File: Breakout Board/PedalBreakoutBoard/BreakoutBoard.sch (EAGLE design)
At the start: 2 parts, among them U1 ES_DAISY_SEED_REV4, X1 5566-8

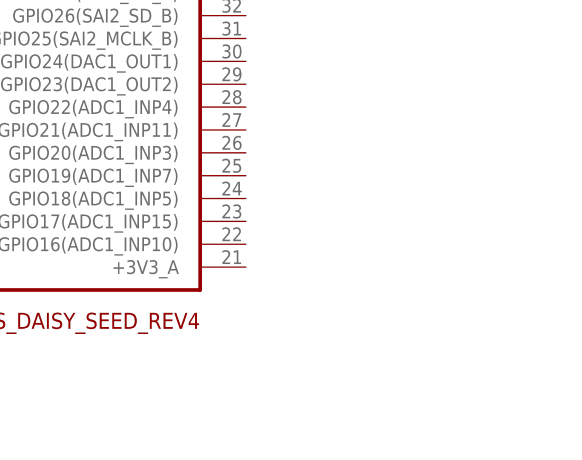
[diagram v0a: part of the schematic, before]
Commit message: DP-16 - Add LED molex
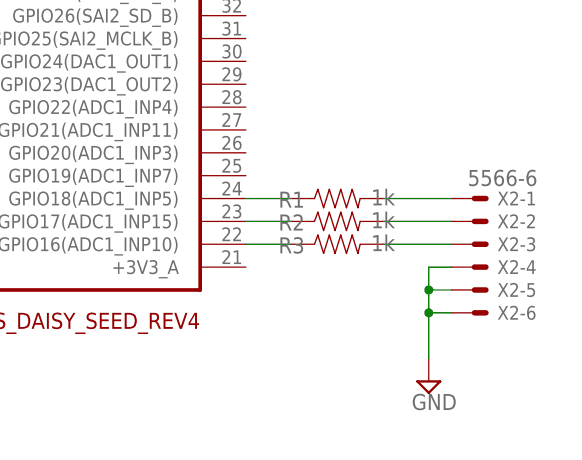
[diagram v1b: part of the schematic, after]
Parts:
- added R1, R2, R3: 1k, SparkFun-Resistors:1KOHM-HORIZ-1/4W-5%
- added X2: 5566-6, con-molex:5566-6
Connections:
- new net N$10: R3.2, X2-3.S
- new net N$5: R1.1, U1.GPIO18(ADC1_INP5)
- new net N$6: R2.1, U1.GPIO17(ADC1_INP15)
- new net N$7: R3.1, U1.GPIO16(ADC1_INP10)
- new net N$8: R1.2, X2-1.S
- new net N$9: R2.2, X2-2.S
- net GND: now also X2-4.S, X2-5.S, X2-6.S
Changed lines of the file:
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@@
 <groups>
 <schematic_group name="AUDIO_MOLEX"/>
+<schematic_group name="LED_MOLEX"/>
 </groups>
 <parts>
@@
 <part name="X1" library="con-molex" library_urn="urn:adsk.eagle:library:165" deviceset="5566-8" device="" package3d_urn="urn:adsk.eagle:package:8078580/1"/>
 <part name="SUPPLY3" library="supply2" library_urn="urn:adsk.eagle:library:372" deviceset="GND" device=""/>
+<part name="X2" library="con-molex" library_urn="urn:adsk.eagle:library:165" deviceset="5566-6" device="" package3d_urn="urn:adsk.eagle:package:8078581/1"/>
+<part name="SUPPLY4" library="supply2" library_urn="urn:adsk.eagle:library:372" deviceset="GND" device=""/>
+<part name="R1" library="SparkFun-Resistors" library_urn="urn:adsk.eagle:library:532" deviceset="1KOHM" device="-HORIZ-1/4W-5%" package3d_urn="urn:adsk.eagle:package:39658/1" value="1k"/>
+<part name="R2" library="SparkFun-Resistors" library_urn="urn:adsk.eagle:library:532" deviceset="1KOHM" device="-HORIZ-1/4W-5%" package3d_urn="urn:adsk.eagle:package:39658/1" value="1k"/>
+<part name="R3" library="SparkFun-Resistors" library_urn="urn:adsk.eagle:library:532" deviceset="1KOHM" device="-HORIZ-1/4W-5%" package3d_urn="urn:adsk.eagle:package:39658/1" value="1k"/>
 </parts>
 <sheets>
@@
 <instance part="SUPPLY3" gate="GND" x="50.8" y="50.8" smashed="yes">
 <attribute name="VALUE" x="48.895" y="47.625" size="1.778" layer="96"/>
+</instance>
+<instance part="X2" gate="-1" x="160.02" y="73.66" smashed="yes" grouprefs="LED_MOLEX">
+<attribute name="NAME" x="162.56" y="72.898" size="1.524" layer="95"/>
+<attribute name="VALUE" x="159.258" y="75.057" size="1.778" layer="96"/>
+</instance>
+<instance part="X2" gate="-2" x="160.02" y="71.12" smashed="yes" grouprefs="LED_MOLEX">
+<attribute name="NAME" x="162.56" y="70.358" size="1.524" layer="95"/>
+</instance>
+<instance part="X2" gate="-3" x="160.02" y="68.58" smashed="yes" grouprefs="LED_MOLEX">
+<attribute name="NAME" x="162.56" y="67.818" size="1.524" layer="95"/>
+</instance>
+<instance part="X2" gate="-4" x="160.02" y="66.04" smashed="yes" grouprefs="LED_MOLEX">
+<attribute name="NAME" x="162.56" y="65.278" size="1.524" layer="95"/>
+</instance>
+<instance part="X2" gate="-5" x="160.02" y="63.5" smashed="yes" grouprefs="LED_MOLEX">
+<attribute name="NAME" x="162.56" y="62.738" size="1.524" layer="95"/>
+</instance>
+<instance part="X2" gate="-6" x="160.02" y="60.96" smashed="yes" grouprefs="LED_MOLEX">
+<attribute name="NAME" x="162.56" y="60.198" size="1.524" layer="95"/>
+</instance>
+<instance part="SUPPLY4" gate="GND" x="154.94" y="53.34" smashed="yes">
+<attribute name="VALUE" x="153.035" y="50.165" size="1.778" layer="96"/>
+</instance>
+<instance part="R1" gate="G$1" x="144.78" y="73.66" smashed="yes">
+<attribute name="NAME" x="139.7" y="72.644" size="1.778" layer="95" font="vector" align="bottom-center"/>
+<attribute name="VALUE" x="149.86" y="74.676" size="1.778" layer="96" font="vector" align="top-center"/>
+</instance>
+<instance part="R2" gate="G$1" x="144.78" y="71.12" smashed="yes">
+<attribute name="NAME" x="139.7" y="70.104" size="1.778" layer="95" font="vector" align="bottom-center"/>
+<attribute name="VALUE" x="149.86" y="72.136" size="1.778" layer="96" font="vector" align="top-center"/>
+</instance>
+<instance part="R3" gate="G$1" x="144.78" y="68.58" smashed="yes">
+<attribute name="NAME" x="139.7" y="67.564" size="1.778" layer="95" font="vector" align="bottom-center"/>
+<attribute name="VALUE" x="149.86" y="69.596" size="1.778" layer="96" font="vector" align="top-center"/>
 </instance>
 </instances>
@@
 <junction x="50.8" y="63.5"/>
 </segment>
+<segment>
+<pinref part="X2" gate="-6" pin="S"/>
+<wire x1="157.48" y1="60.96" x2="154.94" y2="60.96" width="0.1524" layer="91"/>
+<pinref part="SUPPLY4" gate="GND" pin="GND"/>
+<wire x1="154.94" y1="60.96" x2="154.94" y2="55.88" width="0.1524" layer="91"/>
+<pinref part="X2" gate="-5" pin="S"/>
+<wire x1="157.48" y1="63.5" x2="154.94" y2="63.5" width="0.1524" layer="91"/>
+<wire x1="154.94" y1="63.5" x2="154.94" y2="60.96" width="0.1524" layer="91"/>
+<junction x="154.94" y="60.96"/>
+<pinref part="X2" gate="-4" pin="S"/>
+<wire x1="157.48" y1="66.04" x2="154.94" y2="66.04" width="0.1524" layer="91"/>
+<wire x1="154.94" y1="66.04" x2="154.94" y2="63.5" width="0.1524" layer="91"/>
+<junction x="154.94" y="63.5"/>
+</segment>
 </net>
 <net name="N$1" class="0">
@@
 </segment>
 </net>
+<net name="N$5" class="0">
+<segment>
+<pinref part="U1" gate="G$1" pin="GPIO18(ADC1_INP5)"/>
+<pinref part="R1" gate="G$1" pin="1"/>
+<wire x1="134.62" y1="73.66" x2="139.7" y2="73.66" width="0.1524" layer="91"/>
+</segment>
+</net>
+<net name="N$6" class="0">
+<segment>
+<pinref part="U1" gate="G$1" pin="GPIO17(ADC1_INP15)"/>
+<pinref part="R2" gate="G$1" pin="1"/>
+<wire x1="134.62" y1="71.12" x2="139.7" y2="71.12" width="0.1524" layer="91"/>
+</segment>
+</net>
+<net name="N$7" class="0">
+<segment>
+<pinref part="U1" gate="G$1" pin="GPIO16(ADC1_INP10)"/>
+<pinref part="R3" gate="G$1" pin="1"/>
+<wire x1="134.62" y1="68.58" x2="139.7" y2="68.58" width="0.1524" layer="91"/>
+</segment>
+</net>
+<net name="N$8" class="0">
+<segment>
+<pinref part="R1" gate="G$1" pin="2"/>
+<pinref part="X2" gate="-1" pin="S"/>
+<wire x1="149.86" y1="73.66" x2="157.48" y2="73.66" width="0.1524" layer="91"/>
+</segment>
+</net>
+<net name="N$9" class="0">
+<segment>
+<pinref part="R2" gate="G$1" pin="2"/>
+<pinref part="X2" gate="-2" pin="S"/>
+<wire x1="149.86" y1="71.12" x2="157.48" y2="71.12" width="0.1524" layer="91"/>
+</segment>
+</net>
+<net name="N$10" class="0">
+<segment>
+<pinref part="R3" gate="G$1" pin="2"/>
+<pinref part="X2" gate="-3" pin="S"/>
+<wire x1="149.86" y1="68.58" x2="157.48" y2="68.58" width="0.1524" layer="91"/>
+</segment>
+</net>

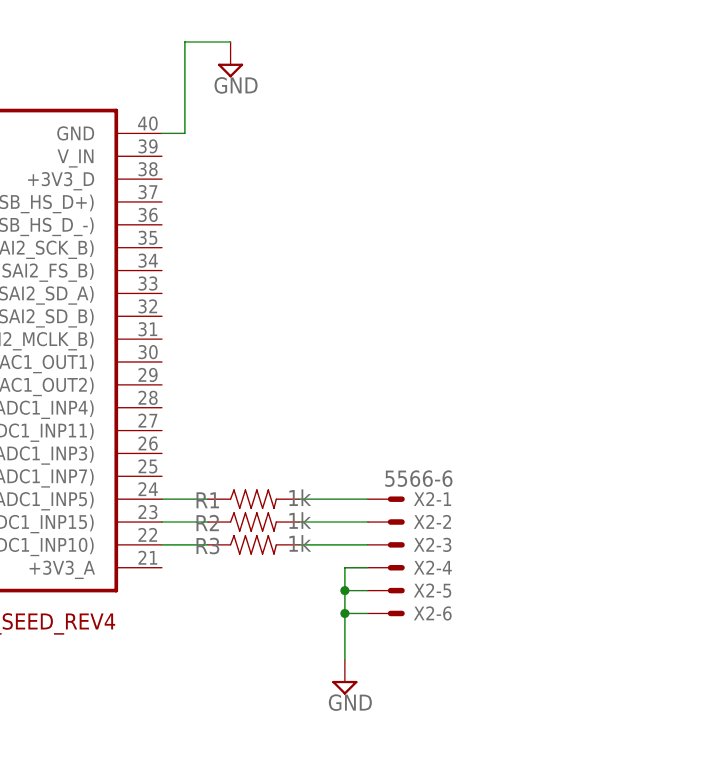
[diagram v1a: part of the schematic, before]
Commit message: DP-16 - Update LED molex
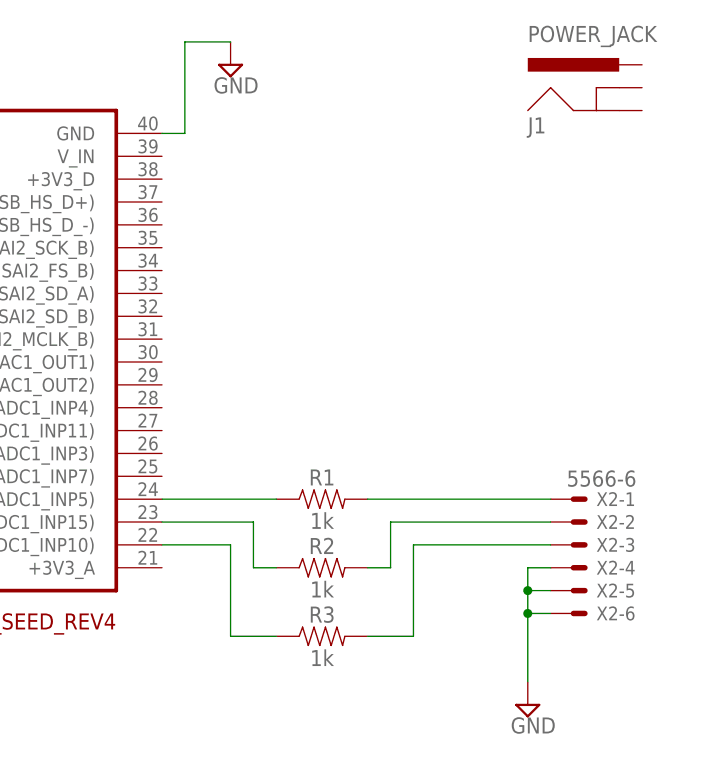
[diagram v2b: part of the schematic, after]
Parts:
- added J1: POWER_JACK, SparkFun-Connectors:POWER_JACK
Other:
- moved on the sheet: R1, R2, R3, X2-1, X2-2, X2-3, X2-4, X2-5, X2-6
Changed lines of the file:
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@@
 <part name="R2" library="SparkFun-Resistors" library_urn="urn:adsk.eagle:library:532" deviceset="1KOHM" device="-HORIZ-1/4W-5%" package3d_urn="urn:adsk.eagle:package:39658/1" value="1k"/>
 <part name="R3" library="SparkFun-Resistors" library_urn="urn:adsk.eagle:library:532" deviceset="1KOHM" device="-HORIZ-1/4W-5%" package3d_urn="urn:adsk.eagle:package:39658/1" value="1k"/>
+<part name="J1" library="SparkFun-Connectors" library_urn="urn:adsk.eagle:library:513" deviceset="POWER_JACK" device="" package3d_urn="urn:adsk.eagle:package:38231/1"/>
 </parts>
 <sheets>
@@
 <attribute name="VALUE" x="48.895" y="47.625" size="1.778" layer="96"/>
 </instance>
-<instance part="X2" gate="-1" x="160.02" y="73.66" smashed="yes" grouprefs="LED_MOLEX">
-<attribute name="NAME" x="162.56" y="72.898" size="1.524" layer="95"/>
-<attribute name="VALUE" x="159.258" y="75.057" size="1.778" layer="96"/>
-</instance>
-<instance part="X2" gate="-2" x="160.02" y="71.12" smashed="yes" grouprefs="LED_MOLEX">
-<attribute name="NAME" x="162.56" y="70.358" size="1.524" layer="95"/>
-</instance>
-<instance part="X2" gate="-3" x="160.02" y="68.58" smashed="yes" grouprefs="LED_MOLEX">
-<attribute name="NAME" x="162.56" y="67.818" size="1.524" layer="95"/>
-</instance>
-<instance part="X2" gate="-4" x="160.02" y="66.04" smashed="yes" grouprefs="LED_MOLEX">
-<attribute name="NAME" x="162.56" y="65.278" size="1.524" layer="95"/>
-</instance>
-<instance part="X2" gate="-5" x="160.02" y="63.5" smashed="yes" grouprefs="LED_MOLEX">
-<attribute name="NAME" x="162.56" y="62.738" size="1.524" layer="95"/>
-</instance>
-<instance part="X2" gate="-6" x="160.02" y="60.96" smashed="yes" grouprefs="LED_MOLEX">
-<attribute name="NAME" x="162.56" y="60.198" size="1.524" layer="95"/>
-</instance>
-<instance part="SUPPLY4" gate="GND" x="154.94" y="53.34" smashed="yes">
-<attribute name="VALUE" x="153.035" y="50.165" size="1.778" layer="96"/>
-</instance>
-<instance part="R1" gate="G$1" x="144.78" y="73.66" smashed="yes">
-<attribute name="NAME" x="139.7" y="72.644" size="1.778" layer="95" font="vector" align="bottom-center"/>
-<attribute name="VALUE" x="149.86" y="74.676" size="1.778" layer="96" font="vector" align="top-center"/>
-</instance>
-<instance part="R2" gate="G$1" x="144.78" y="71.12" smashed="yes">
-<attribute name="NAME" x="139.7" y="70.104" size="1.778" layer="95" font="vector" align="bottom-center"/>
-<attribute name="VALUE" x="149.86" y="72.136" size="1.778" layer="96" font="vector" align="top-center"/>
-</instance>
-<instance part="R3" gate="G$1" x="144.78" y="68.58" smashed="yes">
-<attribute name="NAME" x="139.7" y="67.564" size="1.778" layer="95" font="vector" align="bottom-center"/>
-<attribute name="VALUE" x="149.86" y="69.596" size="1.778" layer="96" font="vector" align="top-center"/>
+<instance part="X2" gate="-1" x="180.34" y="73.66" smashed="yes" grouprefs="LED_MOLEX">
+<attribute name="NAME" x="182.88" y="72.898" size="1.524" layer="95"/>
+<attribute name="VALUE" x="179.578" y="75.057" size="1.778" layer="96"/>
+</instance>
+<instance part="X2" gate="-2" x="180.34" y="71.12" smashed="yes" grouprefs="LED_MOLEX">
+<attribute name="NAME" x="182.88" y="70.358" size="1.524" layer="95"/>
+</instance>
+<instance part="X2" gate="-3" x="180.34" y="68.58" smashed="yes" grouprefs="LED_MOLEX">
+<attribute name="NAME" x="182.88" y="67.818" size="1.524" layer="95"/>
+</instance>
+<instance part="X2" gate="-4" x="180.34" y="66.04" smashed="yes" grouprefs="LED_MOLEX">
+<attribute name="NAME" x="182.88" y="65.278" size="1.524" layer="95"/>
+</instance>
+<instance part="X2" gate="-5" x="180.34" y="63.5" smashed="yes" grouprefs="LED_MOLEX">
+<attribute name="NAME" x="182.88" y="62.738" size="1.524" layer="95"/>
+</instance>
+<instance part="X2" gate="-6" x="180.34" y="60.96" smashed="yes" grouprefs="LED_MOLEX">
+<attribute name="NAME" x="182.88" y="60.198" size="1.524" layer="95"/>
+</instance>
+<instance part="SUPPLY4" gate="GND" x="175.26" y="50.8" smashed="yes">
+<attribute name="VALUE" x="173.355" y="47.625" size="1.778" layer="96"/>
+</instance>
+<instance part="R1" gate="G$1" x="152.4" y="73.66" smashed="yes">
+<attribute name="NAME" x="152.4" y="75.184" size="1.778" layer="95" font="vector" align="bottom-center"/>
+<attribute name="VALUE" x="152.4" y="72.136" size="1.778" layer="96" font="vector" align="top-center"/>
+</instance>
+<instance part="R2" gate="G$1" x="152.4" y="66.04" smashed="yes">
+<attribute name="NAME" x="152.4" y="67.564" size="1.778" layer="95" font="vector" align="bottom-center"/>
+<attribute name="VALUE" x="152.4" y="64.516" size="1.778" layer="96" font="vector" align="top-center"/>
+</instance>
+<instance part="R3" gate="G$1" x="152.4" y="58.42" smashed="yes">
+<attribute name="NAME" x="152.4" y="59.944" size="1.778" layer="95" font="vector" align="bottom-center"/>
+<attribute name="VALUE" x="152.4" y="56.896" size="1.778" layer="96" font="vector" align="top-center"/>
+</instance>
+<instance part="J1" gate="G$1" x="185.42" y="114.3" smashed="yes">
+<attribute name="VALUE" x="175.26" y="124.46" size="1.778" layer="96" font="vector"/>
+<attribute name="NAME" x="175.26" y="114.3" size="1.778" layer="95" font="vector"/>
 </instance>
 </instances>
@@
 <segment>
 <pinref part="X2" gate="-6" pin="S"/>
-<wire x1="157.48" y1="60.96" x2="154.94" y2="60.96" width="0.1524" layer="91"/>
+<wire x1="177.8" y1="60.96" x2="175.26" y2="60.96" width="0.1524" layer="91"/>
 <pinref part="SUPPLY4" gate="GND" pin="GND"/>
-<wire x1="154.94" y1="60.96" x2="154.94" y2="55.88" width="0.1524" layer="91"/>
+<wire x1="175.26" y1="60.96" x2="175.26" y2="53.34" width="0.1524" layer="91"/>
 <pinref part="X2" gate="-5" pin="S"/>
-<wire x1="157.48" y1="63.5" x2="154.94" y2="63.5" width="0.1524" layer="91"/>
-<wire x1="154.94" y1="63.5" x2="154.94" y2="60.96" width="0.1524" layer="91"/>
-<junction x="154.94" y="60.96"/>
+<wire x1="177.8" y1="63.5" x2="175.26" y2="63.5" width="0.1524" layer="91"/>
+<wire x1="175.26" y1="63.5" x2="175.26" y2="60.96" width="0.1524" layer="91"/>
+<junction x="175.26" y="60.96"/>
 <pinref part="X2" gate="-4" pin="S"/>
-<wire x1="157.48" y1="66.04" x2="154.94" y2="66.04" width="0.1524" layer="91"/>
-<wire x1="154.94" y1="66.04" x2="154.94" y2="63.5" width="0.1524" layer="91"/>
-<junction x="154.94" y="63.5"/>
+<wire x1="177.8" y1="66.04" x2="175.26" y2="66.04" width="0.1524" layer="91"/>
+<wire x1="175.26" y1="66.04" x2="175.26" y2="63.5" width="0.1524" layer="91"/>
+<junction x="175.26" y="63.5"/>
 </segment>
 </net>
@@
 <pinref part="U1" gate="G$1" pin="GPIO18(ADC1_INP5)"/>
 <pinref part="R1" gate="G$1" pin="1"/>
-<wire x1="134.62" y1="73.66" x2="139.7" y2="73.66" width="0.1524" layer="91"/>
-</segment>
-</net>
-<net name="N$6" class="0">
-<segment>
-<pinref part="U1" gate="G$1" pin="GPIO17(ADC1_INP15)"/>
-<pinref part="R2" gate="G$1" pin="1"/>
-<wire x1="134.62" y1="71.12" x2="139.7" y2="71.12" width="0.1524" layer="91"/>
-</segment>
-</net>
-<net name="N$7" class="0">
-<segment>
-<pinref part="U1" gate="G$1" pin="GPIO16(ADC1_INP10)"/>
-<pinref part="R3" gate="G$1" pin="1"/>
-<wire x1="134.62" y1="68.58" x2="139.7" y2="68.58" width="0.1524" layer="91"/>
+<wire x1="134.62" y1="73.66" x2="147.32" y2="73.66" width="0.1524" layer="91"/>
 </segment>
 </net>
@@
 <pinref part="R1" gate="G$1" pin="2"/>
 <pinref part="X2" gate="-1" pin="S"/>
-<wire x1="149.86" y1="73.66" x2="157.48" y2="73.66" width="0.1524" layer="91"/>
+<wire x1="157.48" y1="73.66" x2="177.8" y2="73.66" width="0.1524" layer="91"/>
+</segment>
+</net>
+<net name="N$6" class="0">
+<segment>
+<pinref part="U1" gate="G$1" pin="GPIO17(ADC1_INP15)"/>
+<wire x1="134.62" y1="71.12" x2="144.78" y2="71.12" width="0.1524" layer="91"/>
+<wire x1="144.78" y1="71.12" x2="144.78" y2="66.04" width="0.1524" layer="91"/>
+<pinref part="R2" gate="G$1" pin="1"/>
+<wire x1="144.78" y1="66.04" x2="147.32" y2="66.04" width="0.1524" layer="91"/>
+</segment>
+</net>
+<net name="N$7" class="0">
+<segment>
+<pinref part="U1" gate="G$1" pin="GPIO16(ADC1_INP10)"/>
+<wire x1="134.62" y1="68.58" x2="142.24" y2="68.58" width="0.1524" layer="91"/>
+<wire x1="142.24" y1="68.58" x2="142.24" y2="58.42" width="0.1524" layer="91"/>
+<pinref part="R3" gate="G$1" pin="1"/>
+<wire x1="142.24" y1="58.42" x2="147.32" y2="58.42" width="0.1524" layer="91"/>
 </segment>
 </net>
@@
 <segment>
 <pinref part="R2" gate="G$1" pin="2"/>
+<wire x1="157.48" y1="66.04" x2="160.02" y2="66.04" width="0.1524" layer="91"/>
+<wire x1="160.02" y1="66.04" x2="160.02" y2="71.12" width="0.1524" layer="91"/>
 <pinref part="X2" gate="-2" pin="S"/>
-<wire x1="149.86" y1="71.12" x2="157.48" y2="71.12" width="0.1524" layer="91"/>
+<wire x1="160.02" y1="71.12" x2="177.8" y2="71.12" width="0.1524" layer="91"/>
 </segment>
 </net>
@@
 <segment>
 <pinref part="R3" gate="G$1" pin="2"/>
+<wire x1="157.48" y1="58.42" x2="162.56" y2="58.42" width="0.1524" layer="91"/>
+<wire x1="162.56" y1="58.42" x2="162.56" y2="68.58" width="0.1524" layer="91"/>
 <pinref part="X2" gate="-3" pin="S"/>
-<wire x1="149.86" y1="68.58" x2="157.48" y2="68.58" width="0.1524" layer="91"/>
-</segment>
-</net>
+<wire x1="162.56" y1="68.58" x2="177.8" y2="68.58" width="0.1524" layer="91"/>
+</segment>
+</net>
